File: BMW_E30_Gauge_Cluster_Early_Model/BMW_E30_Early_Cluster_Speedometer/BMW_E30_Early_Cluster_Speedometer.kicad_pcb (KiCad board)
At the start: 2 copper layers, 102.5 x 68.3 mm, 36 parts, among them J1 Conn_01x06_Socket, J2 Conn_01x04_Socket, M1 Odometer, Q1 BC327-40, Q2 BD135, U1 UAF2115, U2 UGS 3020

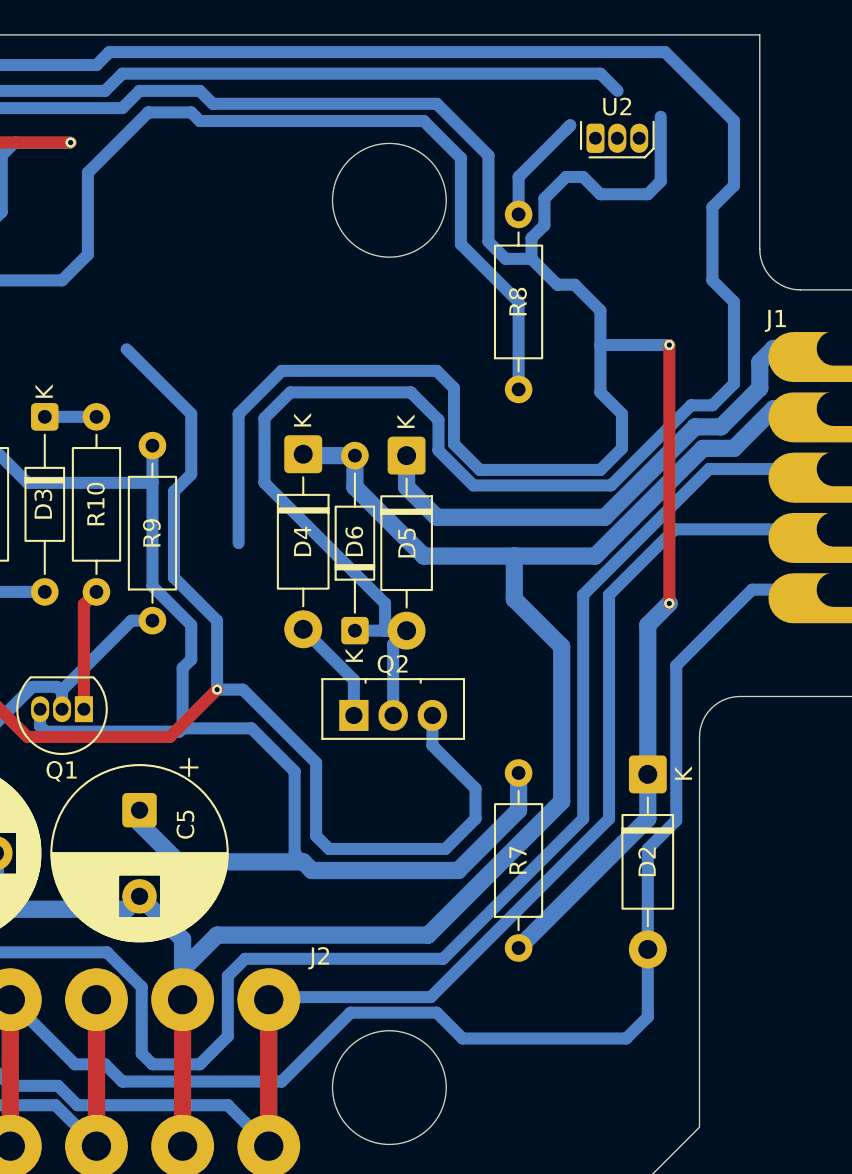
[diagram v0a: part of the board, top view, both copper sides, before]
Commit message: Added Hall Sensor Board
Separate board was added for mounting the Hall effect sensor(s) to the main Speedometer board.
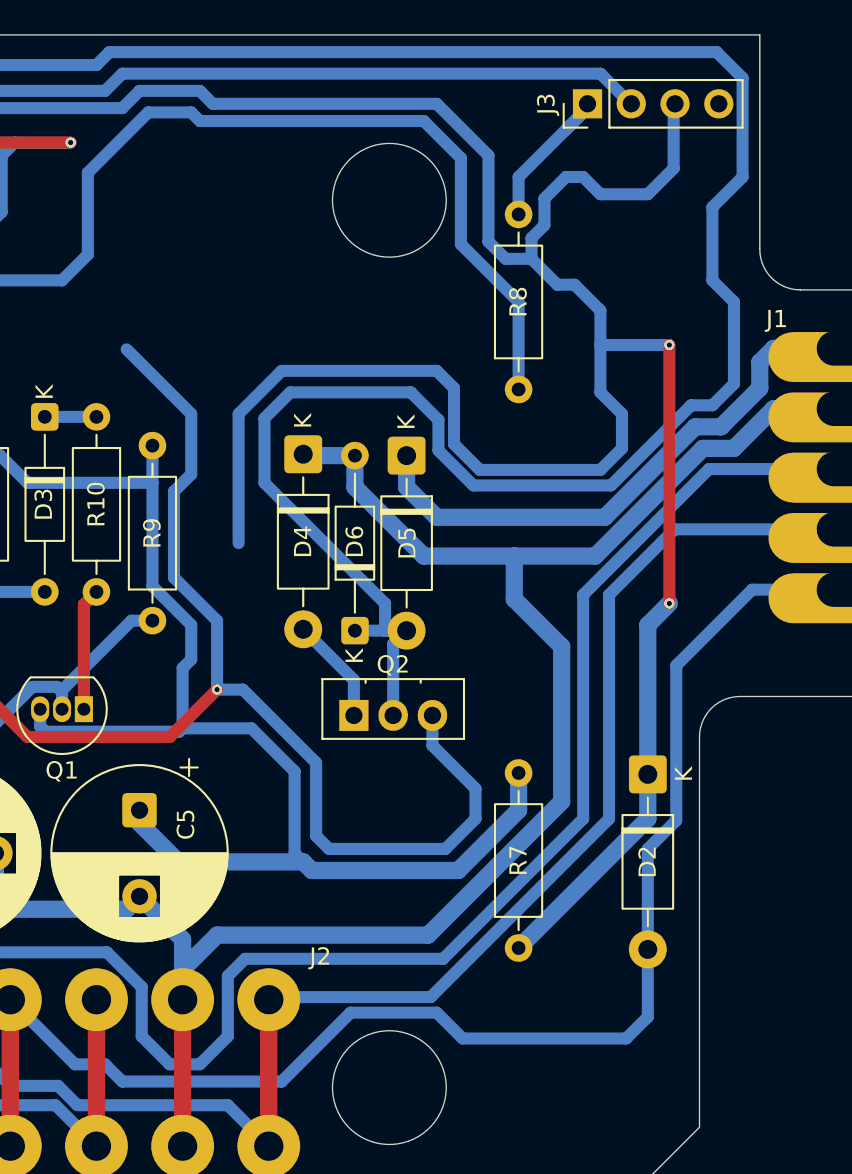
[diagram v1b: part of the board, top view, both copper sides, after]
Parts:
- removed U2: UGS 3020, Package_TO_SOT_THT:TO-92S
- added J3: To Hall effect board, Connector_PinHeader_2.54mm:PinHeader_1x04_P2.54mm_Vertical, F.Cu at (190.0, 39.0)
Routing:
- net Net-(J3-Pin_1): track 6.77 -> 9.84 mm
- net O2_sensor: track 271.4 -> 273.6 mm
- net GND: track 341.7 -> 342.8 mm
- net T15_Protected: track 199.0 -> 200.0 mm
- net Net-(J1-Pin_3): track 166.1 -> 165.5 mm
